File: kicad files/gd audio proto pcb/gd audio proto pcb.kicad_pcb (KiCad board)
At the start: 2 copper layers, 22 parts, among them J1 Vol I2C, J2 SPKR, J3 Ears, U1 MCP4541T, U2 LM4875

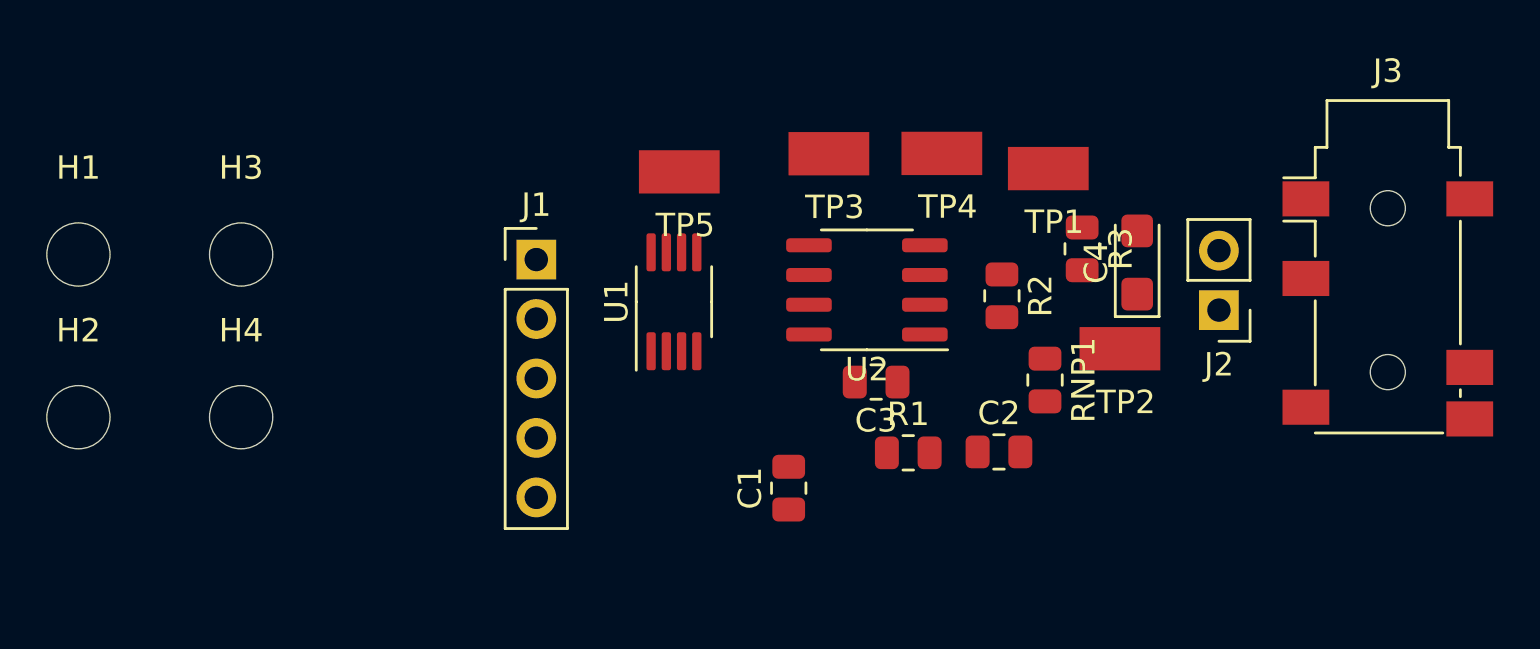
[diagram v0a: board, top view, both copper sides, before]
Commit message: audio (lm4875 test brd) rev1 pcb complete
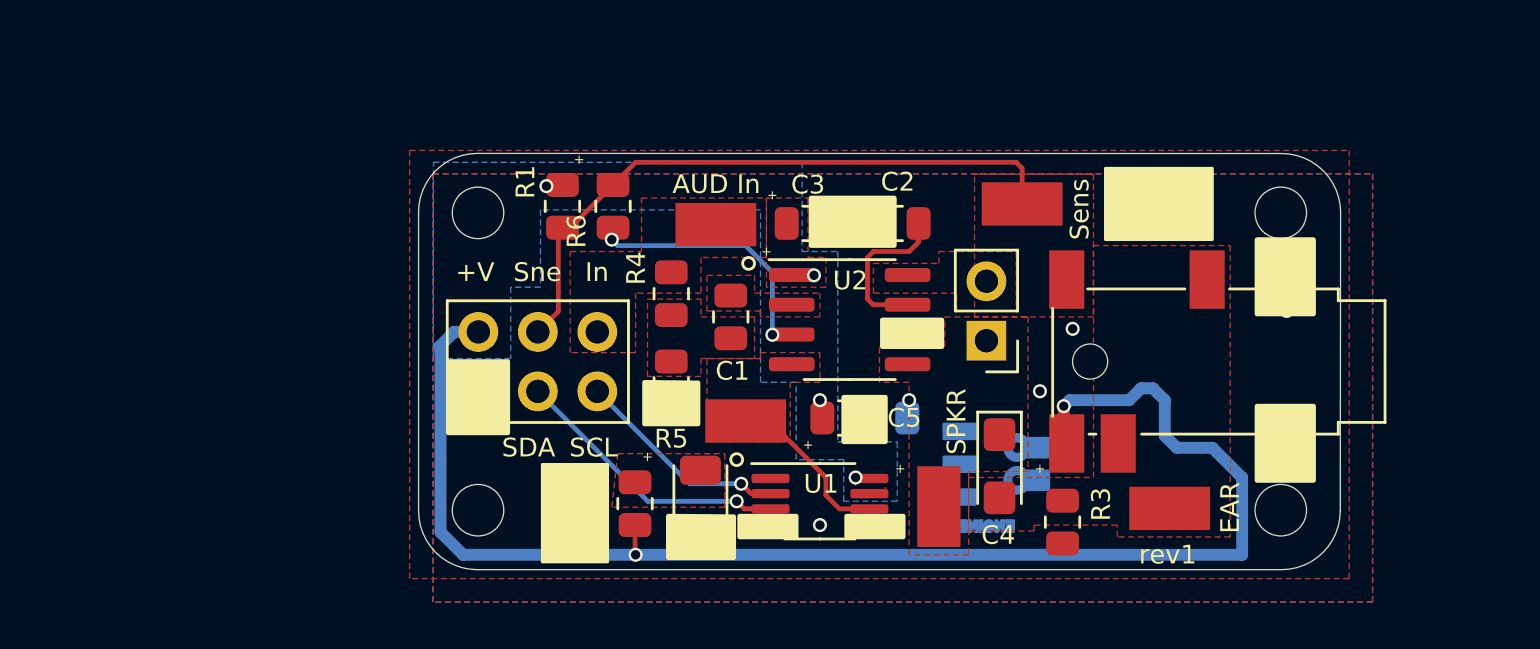
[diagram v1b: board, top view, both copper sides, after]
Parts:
- added C5: 1u, Resistor_SMD:R_0805_2012Metric, F.Cu at (126.7, 109.7)
- added D1: PWR, LED_SMD:LED_1206_3216Metric, F.Cu at (120.6, 113.4)
- added R4: 1, Resistor_SMD:R_0805_2012Metric, F.Cu at (119.4, 104.4)
- added R5: 2, Resistor_SMD:R_0805_2012Metric, F.Cu at (119.4, 108.2)
- added R6: 100k, Resistor_SMD:R_0805_2012Metric, F.Cu at (116.9, 100.7)
- added REF**: OSHW-Symbol_6.7x6mm_SilkScreen, Symbol:OSHW-Symbol_6.7x6mm_SilkScreen, B.Cu at (120.8, 102.4)
- added REF**: KiCad-Logo2_5mm_SilkScreen, Symbol:KiCad-Logo2_5mm_SilkScreen, B.Cu at (141.1, 107.8)
- added TP6: GND, My Libraries:Harwin-S1751-46-Test-Point, F.Cu at (115.3, 113.8)
- added TP7: GND, My Libraries:Harwin-S1751-46-Test-Point, F.Cu at (140.2, 100.6)
- added svg2mod: G***, My Libraries:BE5v2, B.Cu at (135.8, 109.6)
- H1, H2, H3, H4: value MountingHole_M2.5_Screw -> MountingHole_M2_Screw; footprint MountingHole:MountingHole_2.7mm_M2.5 -> MountingHole:MountingHole_2.2mm_M2
- J1: footprint Connector_PinHeader_2.54mm:PinHeader_1x05_P2.54mm_Vertical -> Connector_PinHeader_2.54mm:PinHeader_2x03_P2.54mm_Vertical
- R2: value 100k -> 1k
- RNP1: moved to B.Cu
- moved H2 51.5 mm to (145.4, 113.7)
- moved H1 51.4 mm to (145.4, 101.0)
- moved R1 18.1 mm to (114.7, 100.7), turned to -90 degrees
- moved R2 18.0 mm to (117.8, 113.4)
- moved TP1 15.4 mm to (140.7, 113.6)
- moved R3 11.7 mm to (136.1, 114.2)
- moved TP5 11.0 mm to (122.6, 109.9)
- moved H4 10.9 mm to (111.1, 113.7)
- moved C2 10.7 mm to (129.0, 101.4), turned to 180 degrees
- moved U1 10.6 mm to (125.7, 113.3), turned to 0 degrees
- moved C4 10.5 mm to (133.4, 111.8), turned to -90 degrees
- moved H3 10.3 mm to (111.1, 101.0)
- moved TP2 10.3 mm to (130.8, 113.5), turned to -90 degrees
- moved J2 10.0 mm to (132.8, 106.4)
- moved J3 9.29 mm to (141.0, 107.3), turned to -90 degrees
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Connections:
- C1 pad 1: /WOZ_AUD -> /SCALE_AUD
- J1 pad 1: /Sense -> GND
- J1 pad 2: /WOZ_AUD -> +5V
- J1 pad 4: /AUD_SCL -> /Sense
- J1 pad 5: GND -> /AUD_SCL
- R2 pad 1: Net-(R2-Pad1) -> Net-(D1-Pad2)
- R2 pad 2: /Sense -> +5V
- U2 pad 3: Net-(R2-Pad1) -> Net-(U2-Pad3)
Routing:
- net +5V: track 0.00 -> 61.1 mm, vias 0 -> 6
- net /Sense: track 0.00 -> 27.4 mm
- net /AUD_SDA: track 0.00 -> 12.0 mm, vias 0 -> 1
- net Net-(U2-Pad3): track 0.00 -> 11.5 mm, vias 0 -> 2
- net /AUD_SCL: track 0.00 -> 9.21 mm, vias 0 -> 1
- net /DC_Vol: track 0.00 -> 7.29 mm
- net Net-(C2-Pad1): track 0.00 -> 6.84 mm
- net GND: vias 0 -> 8
- net /SPKR: vias 0 -> 1
- added copper zone on B.Cu, net +5V
- added copper zone on F.Cu, net +5V
- added copper zone on F.Cu, net /DC_Vol
- added copper zone on F.Cu, net /EAR
- added copper zone on F.Cu, net /SCALE_AUD
- added copper zone on F.Cu, net /SPKR
- added copper zone on F.Cu, net /Sense
- added copper zone on F.Cu, net /WOZ_AUD
- added copper zone on B.Cu, net GND
- added copper zone on F.Cu, net GND
- added copper zone on F.Cu, net Net-(C1-Pad2)
- added copper zone on F.Cu, net Net-(D1-Pad2)
- added copper zone on F.Cu, net Net-(J2-Pad2)
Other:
- board outline added: 39.4 x 17.8 mm
- net class Default removed
- board text added: "+"
- board text added: "+V"
- board text added: "AUD In"
- board text added: "EAR"
- board text added: "In"
- board text added: "LM4875 Test board rev1. 2022-01-29 @baldengineer"
- board text added: "SCL"
- board text added: "SDA"
- board text added: "SPKR"
- board text added: "Sens"
- board text added: "Sne"
- board text added: "rev1"

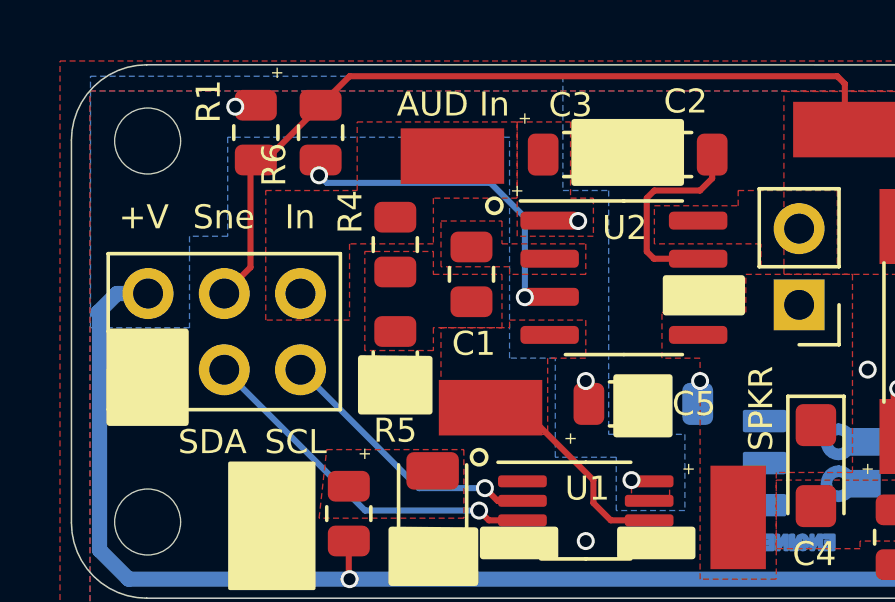
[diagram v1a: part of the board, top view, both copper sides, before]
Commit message: 1206 220nF change and added BOM
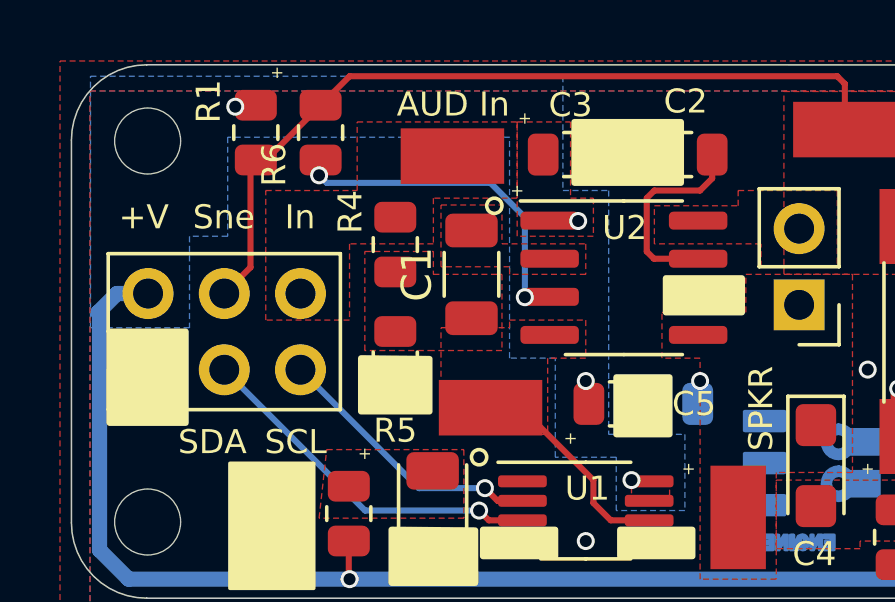
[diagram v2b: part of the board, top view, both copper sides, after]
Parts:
- C1: footprint Resistor_SMD:R_0805_2012Metric -> Resistor_SMD:R_1206_3216Metric

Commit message: Whoops. For that fancy "DRC" feature ...
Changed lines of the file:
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@@
     (property "Sheetname" "")
     (attr smd)
-    (fp_text reference "C1" (at 0 -1.82 90) (layer "F.SilkS")
-      (effects (font (size 1 1) (thickness 0.15)))
+    (fp_text reference "C1" (at -0.09 -0.07 90) (layer "F.SilkS")
+      (effects (font (size 0.6 0.6) (thickness 0.1)))
     )
     (fp_text value "220n" (at 0 1.82 90) (layer "F.Fab")
@@
       (xy 113.8682 111.7092)
     ) (layer "F.SilkS") (width 0.12) (fill solid))
-  (gr_circle (center 122.682 103.124) (end 122.682 103.378) (layer "F.SilkS") (width 0.12) (fill none))
+  (gr_circle (center 123.021 102.925) (end 123.021 103.179) (layer "F.SilkS") (width 0.12) (fill none))
   (gr_poly
     (pts
@@
   (segment (start 118.374 113.284) (end 113.68 108.59) (width 0.2032) (layer "B.Cu") (net 9))
   (segment (start 114.554 105.176) (end 114.554 101.7759) (width 0.2032) (layer "F.Cu") (net 11))
-  (segment (start 116.8908 99.7731) (end 117.8579 98.806) (width 0.2032) (layer "F.Cu") (net 11))
   (segment (start 134.112 98.806) (end 134.366 99.06) (width 0.2032) (layer "F.Cu") (net 11))
   (segment (start 115.0658 101.5981) (end 116.8908 99.7731) (width 0.2032) (layer "F.Cu") (net 11))
+  (segment (start 117.8579 98.806) (end 134.112 98.806) (width 0.2032) (layer "F.Cu") (net 11))
   (segment (start 113.68 106.05) (end 114.554 105.176) (width 0.2032) (layer "F.Cu") (net 11))
-  (segment (start 134.366 99.06) (end 134.366 100.584) (width 0.2032) (layer "F.Cu") (net 11))
   (segment (start 114.554 101.7759) (end 114.7318 101.5981) (width 0.2032) (layer "F.Cu") (net 11))
+  (segment (start 134.366 99.06) (end 134.366 100.584) (width 0.2032) (layer "F.Cu") (net 11))
   (segment (start 114.7318 101.5981) (end 115.0658 101.5981) (width 0.2032) (layer "F.Cu") (net 11))
-  (segment (start 116.84 99.7223) (end 116.8908 99.7731) (width 0.2032) (layer "F.Cu") (net 11))
-  (segment (start 117.8579 98.806) (end 134.112 98.806) (width 0.2032) (layer "F.Cu") (net 11))
+  (segment (start 117.8579 98.806) (end 116.8908 99.7731) (width 0.2032) (layer "F.Cu") (net 11))
   (segment (start 125.984 113.03) (end 125.984 112.268) (width 0.2032) (layer "F.Cu") (net 12))
   (segment (start 126.563 113.609) (end 125.984 113.03) (width 0.2032) (layer "F.Cu") (net 12))
@@
         (xy 122.936 107.95)
         (xy 120.65 107.95)
-        (xy 120.65 107.95)
         (xy 118.364 107.95)
         (xy 118.364 104.648)
@@
     (polygon
       (pts
-        (xy 149.336 117.586)
-        (xy 109.204 117.586)
-        (xy 109.204 99.298)
-        (xy 149.336 99.298)
+        (xy 149.286 116.925)
+        (xy 106.879 116.925)
+        (xy 106.879 97.512)
+        (xy 149.286 97.512)
       )
     )
@@
   )
   (zone (net 6) (net_name "/EAR") (layer "F.Cu") (hatch edge 0.508)
-    (priority 2)
+    (priority 3)
     (connect_pads yes (clearance 0.254))
     (min_thickness 0.127) (filled_areas_thickness no)
@@
       )
     )
-  )
-  (zone (net 3) (net_name "GND") (layer "F.Cu") (hatch edge 0.508)
-    (connect_pads thru_hole_only (clearance 0.254))
-    (min_thickness 0.127) (filled_areas_thickness no)
-    (fill yes (thermal_gap 0.254) (thermal_bridge_width 0.508))
-    (polygon
-      (pts
-        (xy 148.336 116.586)
-        (xy 108.204 116.586)
-        (xy 108.204 98.298)
-        (xy 148.336 98.298)
-      )
-    )

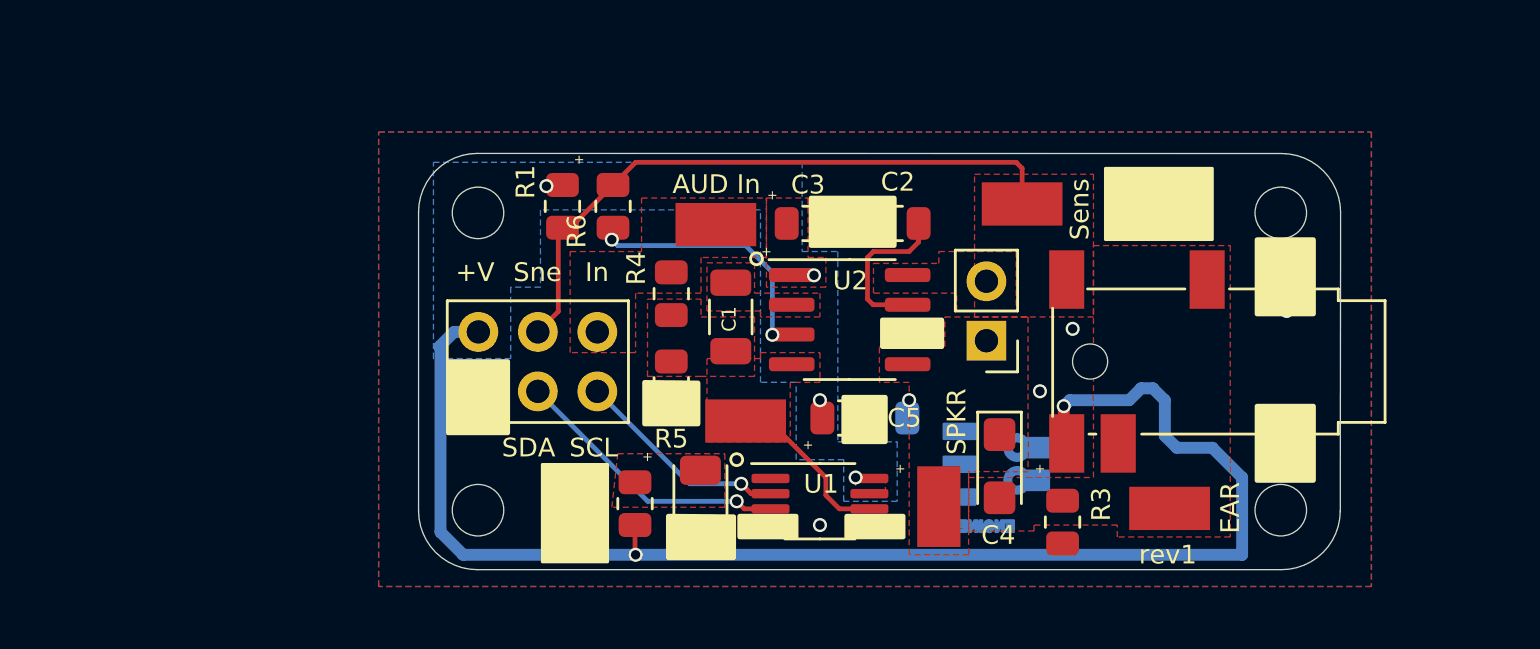
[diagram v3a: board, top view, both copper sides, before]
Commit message: fixed Headphone sense before generating gerbers
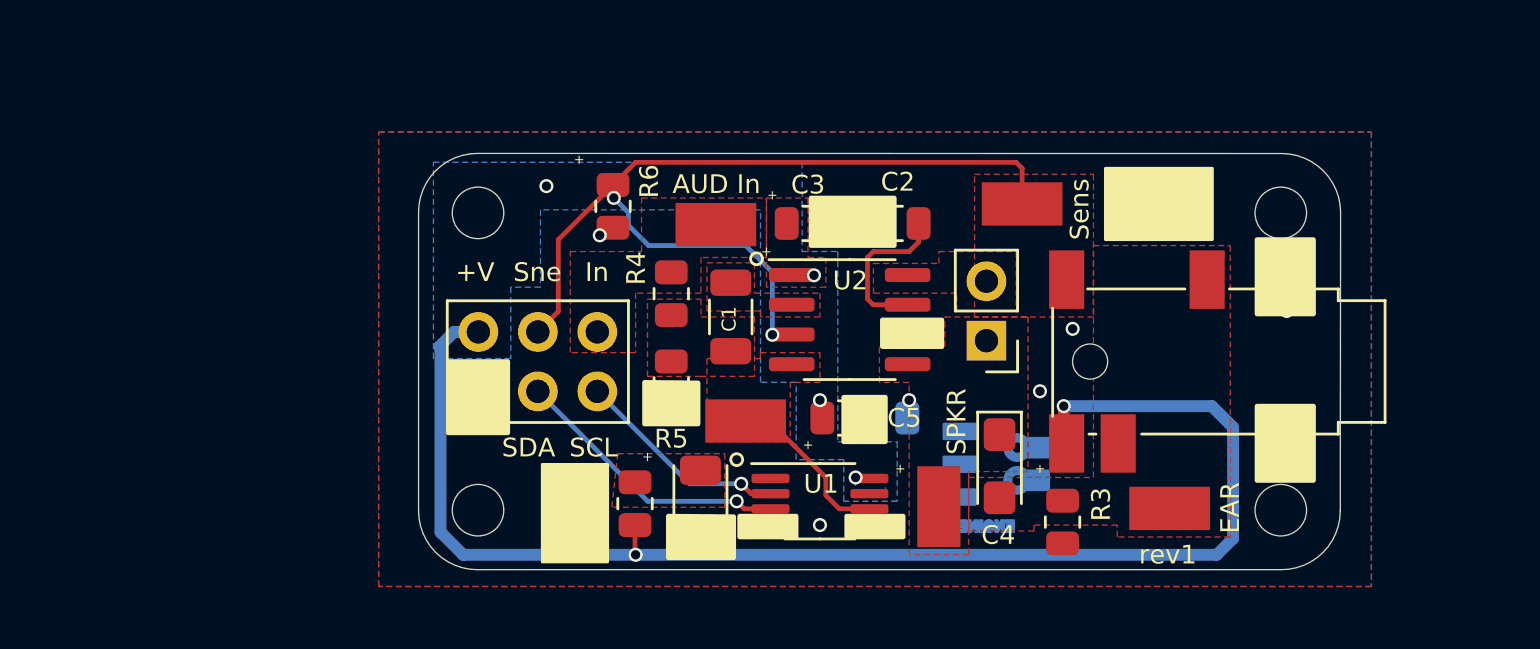
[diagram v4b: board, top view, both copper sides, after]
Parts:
- removed R1: 100k, Resistor_SMD:R_0805_2012Metric
- R6: value 100k -> 10k
- turned R6 to 90 degrees
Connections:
- R6 pad 1: /Sense -> GND
- R6 pad 2: Net-(R6-Pad2) -> /Sense
- U2 pad 3: Net-(R6-Pad2) -> /Sense
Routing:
- net /Sense: track 27.3 -> 39.6 mm, vias 0 -> 2
- net Net-(R6-Pad2): track 11.5 -> 0.00 mm, vias 2 -> 0
- net +5V: track 61.1 -> 59.7 mm
- net GND: track 0.00 -> 0.07 mm, vias 8 -> 9
